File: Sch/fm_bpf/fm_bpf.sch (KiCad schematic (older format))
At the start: 28 parts, among them CN1 SMA_Edge, CN2 SMA_Edge, J1 JP2, U1 LP5907_SOT-23, U2 PSA4-5043+

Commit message: PCB layout in progress
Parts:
- removed J1: JP2, adc_lib:M20-9980245, symbol JP2
- added W1, W2: TEST_1P, adc_lib:68000-401HLF, symbol TEST_1P
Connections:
- net labels removed: +3V3
- wire segments 57 -> 49
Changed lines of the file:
@@
 $EndDescr
 $Comp
-L JP2 J1
-U 1 1 597848E9
-P 1600 5000
-F 0 "J1" H 1600 4750 60  0000 C CNN
-F 1 "JP2" H 1600 5200 60  0000 C CNN
-F 2 "adc_lib:M20-9980245" H 1550 5100 60  0001 C CNN
-F 3 "" H 1550 5100 60  0001 C CNN
-	1    1600 5000
-	1    0    0    -1
-$EndComp
-$Comp
-L +3V3 #PWR01
-U 1 1 59784946
-P 1050 4850
-F 0 "#PWR01" H 1050 4700 50  0001 C CNN
-F 1 "+3V3" H 1050 4990 50  0000 C CNN
-F 2 "" H 1050 4850 50  0000 C CNN
-F 3 "" H 1050 4850 50  0000 C CNN
-	1    1050 4850
-	1    0    0    -1
-$EndComp
-$Comp
-L +5V #PWR02
+L +5V #PWR01
 U 1 1 59784960
-P 2100 4850
-F 0 "#PWR02" H 2100 4700 50  0001 C CNN
-F 1 "+5V" H 2100 4990 50  0000 C CNN
-F 2 "" H 2100 4850 50  0000 C CNN
-F 3 "" H 2100 4850 50  0000 C CNN
-	1    2100 4850
-	1    0    0    -1
-$EndComp
-$Comp
-L GND #PWR03
-U 1 1 597849CB
-P 1050 5350
-F 0 "#PWR03" H 1050 5100 50  0001 C CNN
-F 1 "GND" H 1050 5200 50  0000 C CNN
-F 2 "" H 1050 5350 50  0000 C CNN
-F 3 "" H 1050 5350 50  0000 C CNN
-	1    1050 5350
+P 1900 4250
+F 0 "#PWR01" H 1900 4100 50  0001 C CNN
+F 1 "+5V" H 1900 4390 50  0000 C CNN
+F 2 "" H 1900 4250 50  0000 C CNN
+F 3 "" H 1900 4250 50  0000 C CNN
+	1    1900 4250
 	1    0    0    -1
 $EndComp
@@
 $EndComp
 $Comp
-L GND #PWR04
+L GND #PWR02
 U 1 1 59784C9E
 P 1650 3250
-F 0 "#PWR04" H 1650 3000 50  0001 C CNN
+F 0 "#PWR02" H 1650 3000 50  0001 C CNN
 F 1 "GND" H 1650 3100 50  0000 C CNN
 F 2 "" H 1650 3250 50  0000 C CNN
@@
 $EndComp
 $Comp
-L GND #PWR05
+L GND #PWR03
 U 1 1 5979F3B6
 P 2400 2100
-F 0 "#PWR05" H 2400 1850 50  0001 C CNN
+F 0 "#PWR03" H 2400 1850 50  0001 C CNN
 F 1 "GND" H 2400 1950 50  0000 C CNN
 F 2 "" H 2400 2100 50  0000 C CNN
@@
 NoConn ~ 3350 1700
 $Comp
-L +5V #PWR06
+L +5V #PWR04
 U 1 1 5979F65E
 P 2050 1350
-F 0 "#PWR06" H 2050 1200 50  0001 C CNN
+F 0 "#PWR04" H 2050 1200 50  0001 C CNN
 F 1 "+5V" H 2050 1490 50  0000 C CNN
 F 2 "" H 2050 1350 50  0000 C CNN
@@
 $EndComp
 $Comp
-L GND #PWR07
+L GND #PWR05
 U 1 1 5979F98F
 P 4200 2050
-F 0 "#PWR07" H 4200 1800 50  0001 C CNN
+F 0 "#PWR05" H 4200 1800 50  0001 C CNN
 F 1 "GND" H 4200 1900 50  0000 C CNN
 F 2 "" H 4200 2050 50  0000 C CNN
@@
 $EndComp
 $Comp
-L GND #PWR08
+L GND #PWR06
 U 1 1 5979FA91
 P 5200 2050
-F 0 "#PWR08" H 5200 1800 50  0001 C CNN
+F 0 "#PWR06" H 5200 1800 50  0001 C CNN
 F 1 "GND" H 5200 1900 50  0000 C CNN
 F 2 "" H 5200 2050 50  0000 C CNN
@@
 $EndComp
 $Comp
-L GND #PWR09
+L GND #PWR07
 U 1 1 597A0121
 P 4600 3250
-F 0 "#PWR09" H 4600 3000 50  0001 C CNN
+F 0 "#PWR07" H 4600 3000 50  0001 C CNN
 F 1 "GND" H 4600 3100 50  0000 C CNN
 F 2 "" H 4600 3250 50  0000 C CNN
@@
 	1    0    0    -1
 $EndComp
-Wire Wire Line
-	1050 4850 1050 5000
-Wire Wire Line
-	1050 5000 1250 5000
-Wire Wire Line
-	2100 5000 1950 5000
-Wire Wire Line
-	2100 4850 2100 5000
-Wire Wire Line
-	1950 5100 2100 5100
-Wire Wire Line
-	2100 5100 2100 5350
-Wire Wire Line
-	2100 5350 1050 5350
-Wire Wire Line
-	1050 5350 1050 5100
-Wire Wire Line
-	1050 5100 1250 5100
 Wire Wire Line
 	1850 2700 1650 2700
@@
 $EndComp
 $Comp
-L GND #PWR010
+L GND #PWR08
 U 1 1 597A07B7
 P 2750 3200
-F 0 "#PWR010" H 2750 2950 50  0001 C CNN
+F 0 "#PWR08" H 2750 2950 50  0001 C CNN
 F 1 "GND" H 2750 3050 50  0000 C CNN
 F 2 "" H 2750 3200 50  0000 C CNN
@@
 	6400 2700 6400 3000
 $Comp
-L GND #PWR011
+L GND #PWR09
 U 1 1 597A19E1
 P 7450 3750
-F 0 "#PWR011" H 7450 3500 50  0001 C CNN
+F 0 "#PWR09" H 7450 3500 50  0001 C CNN
 F 1 "GND" H 7450 3600 50  0000 C CNN
 F 2 "" H 7450 3750 50  0000 C CNN
@@
 Connection ~ 8700 3000
 $Comp
-L GND #PWR012
+L GND #PWR010
 U 1 1 597A2125
 P 9850 3400
-F 0 "#PWR012" H 9850 3150 50  0001 C CNN
+F 0 "#PWR010" H 9850 3150 50  0001 C CNN
 F 1 "GND" H 9850 3250 50  0000 C CNN
 F 2 "" H 9850 3400 50  0000 C CNN
@@
 Connection ~ 2050 1500
 $Comp
-L PWR_FLAG #FLG013
+L PWR_FLAG #FLG011
 U 1 1 597B088B
-P 2450 4850
-F 0 "#FLG013" H 2450 4945 50  0001 C CNN
-F 1 "PWR_FLAG" H 2450 5030 50  0000 C CNN
-F 2 "" H 2450 4850 50  0000 C CNN
-F 3 "" H 2450 4850 50  0000 C CNN
-	1    2450 4850
-	1    0    0    -1
-$EndComp
-Wire Wire Line
-	2450 4850 2450 4900
-Wire Wire Line
-	2450 4900 2100 4900
-Connection ~ 2100 4900
+P 1900 4400
+F 0 "#FLG011" H 1900 4495 50  0001 C CNN
+F 1 "PWR_FLAG" H 1900 4580 50  0000 C CNN
+F 2 "" H 1900 4400 50  0000 C CNN
+F 3 "" H 1900 4400 50  0000 C CNN
+	1    1900 4400
+	0    1    1    0
+$EndComp
 Text Notes 4500 2000 0    60   ~ 0
 410mOhm
@@
 	-1   0    0    1
 $EndComp
+$Comp
+L TEST_1P W2
+U 1 1 597F2952
+P 1600 4300
+F 0 "W2" H 1600 4570 50  0000 C CNN
+F 1 "TEST_1P" H 1600 4500 50  0000 C CNN
+F 2 "adc_lib:68000-401HLF" H 1800 4300 50  0001 C CNN
+F 3 "" H 1800 4300 50  0000 C CNN
+	1    1600 4300
+	1    0    0    -1
+$EndComp
+Wire Wire Line
+	1600 4300 1600 4400
+Wire Wire Line
+	1600 4400 1900 4400
+Wire Wire Line
+	1900 4400 1900 4250
+$Comp
+L TEST_1P W1
+U 1 1 597F2E3D
+P 1150 4300
+F 0 "W1" H 1150 4570 50  0000 C CNN
+F 1 "TEST_1P" H 1150 4500 50  0000 C CNN
+F 2 "adc_lib:68000-401HLF" H 1350 4300 50  0001 C CNN
+F 3 "" H 1350 4300 50  0000 C CNN
+	1    1150 4300
+	1    0    0    -1
+$EndComp
+$Comp
+L GND #PWR012
+U 1 1 597F2E81
+P 1150 4300
+F 0 "#PWR012" H 1150 4050 50  0001 C CNN
+F 1 "GND" H 1150 4150 50  0000 C CNN
+F 2 "" H 1150 4300 50  0000 C CNN
+F 3 "" H 1150 4300 50  0000 C CNN
+	1    1150 4300
+	1    0    0    -1
+$EndComp
 $EndSCHEMATC

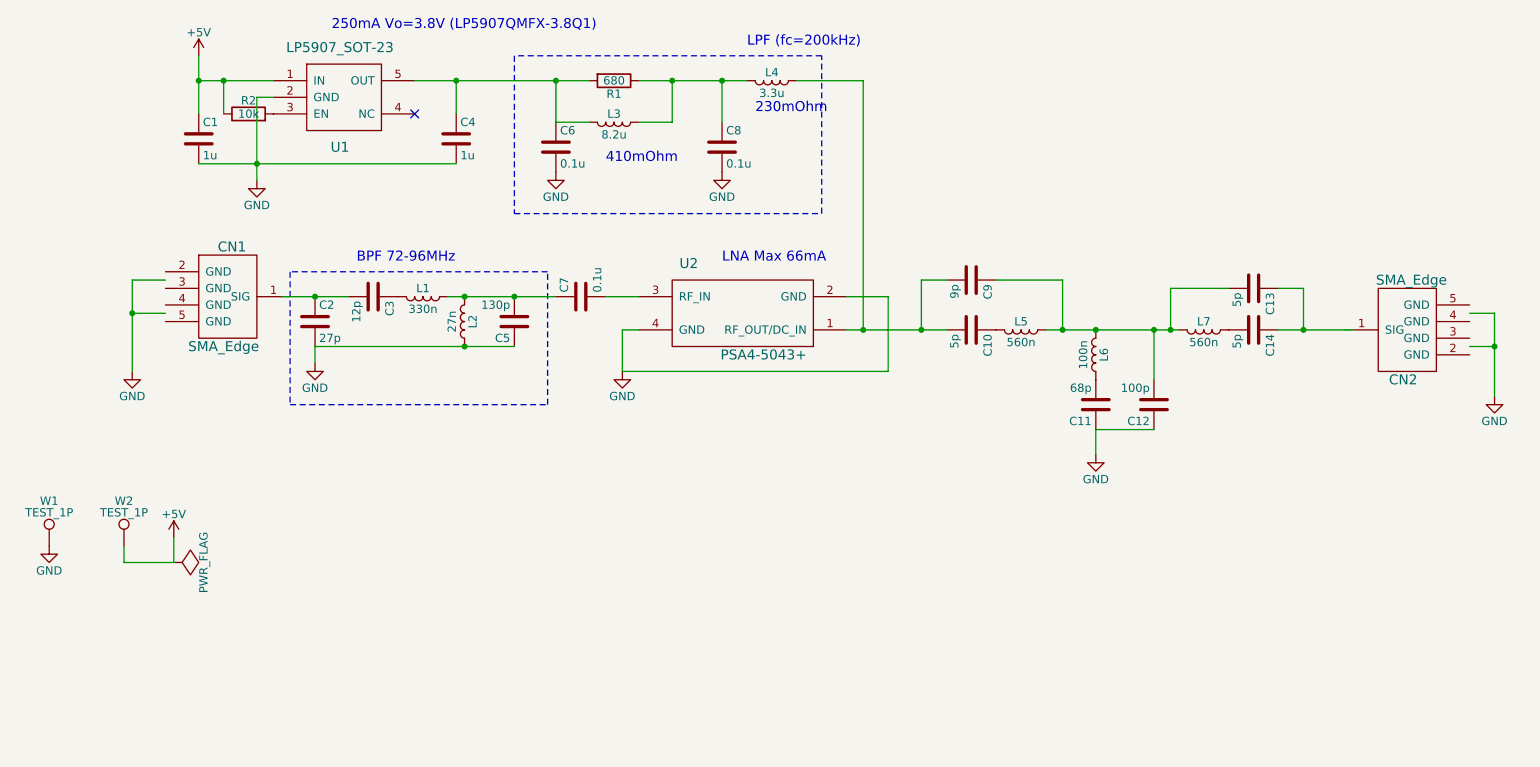
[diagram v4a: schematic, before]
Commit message: Fix BOM for BPF and layout
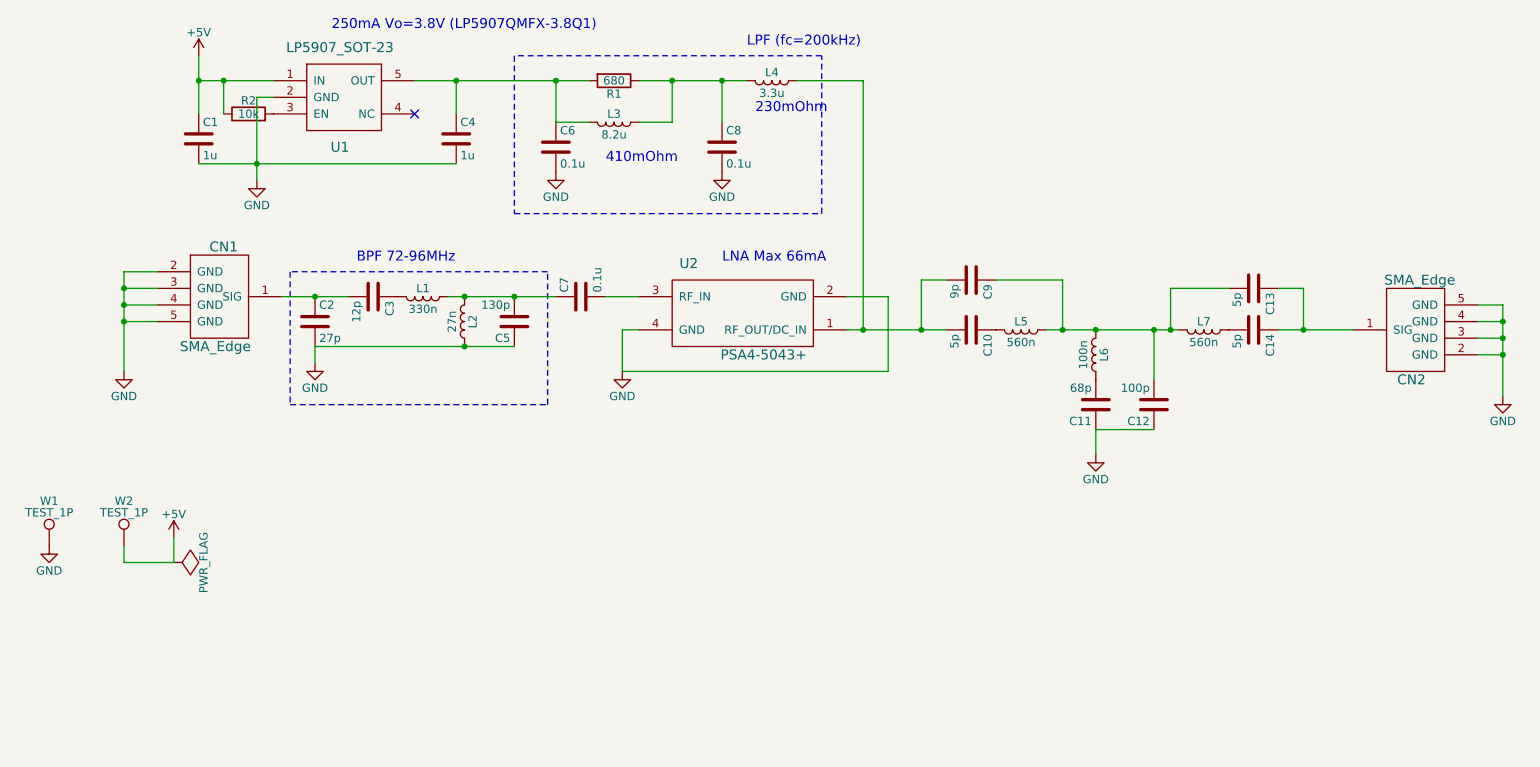
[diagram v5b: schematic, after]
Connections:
- wire segments 49 -> 53
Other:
- moved on the sheet: CN1, CN2
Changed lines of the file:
@@
 L GND #PWR02
 U 1 1 59784C9E
-P 1650 3250
-F 0 "#PWR02" H 1650 3000 50  0001 C CNN
-F 1 "GND" H 1650 3100 50  0000 C CNN
-F 2 "" H 1650 3250 50  0000 C CNN
-F 3 "" H 1650 3250 50  0000 C CNN
-	1    1650 3250
+P 1600 3250
+F 0 "#PWR02" H 1600 3000 50  0001 C CNN
+F 1 "GND" H 1600 3100 50  0000 C CNN
+F 2 "" H 1600 3250 50  0000 C CNN
+F 3 "" H 1600 3250 50  0000 C CNN
+	1    1600 3250
 	1    0    0    -1
 $EndComp
@@
 $EndComp
 Wire Wire Line
-	1850 2700 1650 2700
-Wire Wire Line
-	1650 2700 1650 3250
-Wire Wire Line
-	1850 2900 1650 2900
-Connection ~ 1650 2900
+	1600 2650 1600 3250
 Wire Wire Line
 	2500 1600 2400 1600
@@
 L GND #PWR010
 U 1 1 597A2125
-P 9850 3400
-F 0 "#PWR010" H 9850 3150 50  0001 C CNN
-F 1 "GND" H 9850 3250 50  0000 C CNN
-F 2 "" H 9850 3400 50  0000 C CNN
-F 3 "" H 9850 3400 50  0000 C CNN
-	1    9850 3400
-	1    0    0    -1
-$EndComp
-Wire Wire Line
-	9850 2900 9850 3400
-Wire Wire Line
-	9700 3100 9850 3100
-Connection ~ 9850 3100
-Wire Wire Line
-	9700 2900 9850 2900
+P 9900 3400
+F 0 "#PWR010" H 9900 3150 50  0001 C CNN
+F 1 "GND" H 9900 3250 50  0000 C CNN
+F 2 "" H 9900 3400 50  0000 C CNN
+F 3 "" H 9900 3400 50  0000 C CNN
+	1    9900 3400
+	1    0    0    -1
+$EndComp
+Wire Wire Line
+	9900 2850 9900 3400
 Wire Notes Line
 	3950 1350 3950 2300
@@
 L SMA_Edge CN1
 U 1 1 597C80E9
-P 2200 2800
-F 0 "CN1" H 2250 3100 60  0000 C CNN
-F 1 "SMA_Edge" H 2200 2500 60  0000 C CNN
-F 2 "adc_lib:SMA_Edge" H 2200 2800 60  0001 C CNN
-F 3 "" H 2200 2800 60  0001 C CNN
-	1    2200 2800
+P 2150 2800
+F 0 "CN1" H 2200 3100 60  0000 C CNN
+F 1 "SMA_Edge" H 2150 2500 60  0000 C CNN
+F 2 "adc_lib:SMA_Edge" H 2150 2800 60  0001 C CNN
+F 3 "" H 2150 2800 60  0001 C CNN
+	1    2150 2800
 	1    0    0    -1
 $EndComp
@@
 L SMA_Edge CN2
 U 1 1 597C8478
-P 9350 3000
-F 0 "CN2" H 9400 3300 60  0000 C CNN
-F 1 "SMA_Edge" H 9350 2700 60  0000 C CNN
-F 2 "adc_lib:SMA_Edge" H 9350 3000 60  0001 C CNN
-F 3 "" H 9350 3000 60  0001 C CNN
-	1    9350 3000
+P 9400 3000
+F 0 "CN2" H 9450 3300 60  0000 C CNN
+F 1 "SMA_Edge" H 9400 2700 60  0000 C CNN
+F 2 "adc_lib:SMA_Edge" H 9400 3000 60  0001 C CNN
+F 3 "" H 9400 3000 60  0001 C CNN
+	1    9400 3000
 	-1   0    0    1
 $EndComp
@@
 	1    0    0    -1
 $EndComp
+Wire Wire Line
+	1600 2650 1800 2650
+Wire Wire Line
+	1800 2750 1600 2750
+Connection ~ 1600 2750
+Wire Wire Line
+	1800 2850 1600 2850
+Connection ~ 1600 2850
+Wire Wire Line
+	1800 2950 1600 2950
+Connection ~ 1600 2950
+Wire Wire Line
+	9750 2850 9900 2850
+Wire Wire Line
+	9750 2950 9900 2950
+Connection ~ 9900 2950
+Wire Wire Line
+	9750 3050 9900 3050
+Connection ~ 9900 3050
+Wire Wire Line
+	9750 3150 9900 3150
+Connection ~ 9900 3150
 $EndSCHEMATC
